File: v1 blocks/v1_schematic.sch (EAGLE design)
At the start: 209 parts, among them IC1 PCA82C250, IC2 FT232RL, IC3 SP3223EBP, IC4 MAX481CPA, IC5 LM2576T, Q1 25MHz, Q2 32.768kHz, Q3 2N2222A, T1 ST02-3.5MM, T3 2N2222, T4 2N2222, T5 2N2222, T6 2N2222, T7 2N2222, U1 ON_SEMICONDUCTOR_NCP1117ST33T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, U2 ON_SEMICONDUCTOR_NCP1117ST50T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, X1 MINI-USB-32005-201, X10 PC817SW, X11 PC817SW, X12 PC817SW, X13 PC817SW, X14 PC817SW, X15 PC817SW, X16 PC817SW, X17 PC817SW, X18 PC817SW, X19 PC817SW, X20 PC817SW, X21 PC817SW, X22 PC817SW, X23 PC817SW, X24 PC817SW, X6 SDBMF, X7 5566-8, X8 5566-8, X9 PC817SW

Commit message: V2
Created new layout template
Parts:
- removed J1: (no value), con-lsta:JBK20
- removed T3, T4, T5, T6, T7: 2N2222, transistor-neu-to92:2N2222
- added H1, H2, H3: MOUNT-PAD-ROUND3.2, holes:MOUNT-PAD-ROUND3.2
- added Q4, Q5, Q6, Q7, Q8: (no value), semicon-smd-ipc:NPN-TRANSISTOR_SOT23
- added U$3: MICROSD-PUSH-OUT, microsd:MICROSD-PUSH-OUT
- X6: value SDBMF -> 5566-20; device farnell:SDBMF -> con-molex:5566-20
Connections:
- net +3V3: now also U$3.VDD, X6-1.S, X6-2.S; no longer J1.1, J1.2, R30.1, R31.1, R32.1, R33.1, R34.2, R35.2, X6.4
- net GND: now also Q8.E, R30.1, R31.1, R32.1, R33.1, R34.2, R35.2, U$3.VSS, X6-10.S, X6-12.S, X6-14.S, X6-16.S, X6-18.S, X6-20.S, X6-4.S, X6-6.S, X6-8.S; no longer J1.10, J1.12, J1.14, J1.16, J1.18, J1.20, J1.4, J1.6, J1.8, T7.E, X6.3, X6.6
- net GND2: now also Q8.C; no longer T7.C
- net N$49: now also Q4.B; no longer T3.B
- net N$50: now also X6-11.S; no longer J1.11
- net N$51: now also Q5.B; no longer T4.B
- net N$52: now also Q6.B; no longer T5.B
- net N$53: now also X6-17.S; no longer J1.17
- net N$54: now also Q7.B; no longer T6.B
- net N$55: now also Q8.B; no longer T7.B
- net N$56: now also X6-19.S; no longer J1.19
- net NRF_SCK: now also X6-13.S; no longer J1.13
- net R1IN: now also Q7.E; no longer T6.E
- net R1IN_: now also Q7.C; no longer T6.C
- net R2IN: now also Q5.E; no longer T4.E
- net R2IN_: now also Q5.C; no longer T4.C
- net RESET#: now also X6-15.S; no longer J1.15
- net SD_CMD: now also U$3.CMD_DIN; no longer X6.2
- net SD_D0: now also U$3.DAT0_DO; no longer X6.7
- net SD_D1: now also U$3.DAT1; no longer X6.8
- net SD_D2: now also U$3.DAT2; no longer X6.9
- net SD_D3: now also U$3.CD_DAT3_CS; no longer X6.1
- net SD_SCK: now also U$3.CLK; no longer X6.5
- net T1OUT: now also Q6.E; no longer T5.E
- net T1OUT_: now also Q6.C; no longer T5.C
- net T2OUT: now also Q4.E; no longer T3.E
- net T2OUT_: now also Q4.C; no longer T3.C
- net TCK/SWCLK: now also X6-9.S; no longer J1.9
- net TDI: now also X6-5.S; no longer J1.5
- net TMS/SWDIO: now also X6-7.S; no longer J1.7
- net TRST: now also X6-3.S; no longer J1.3
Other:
- moved on the sheet: C52, R30, R31, R32, R33, R34, R35

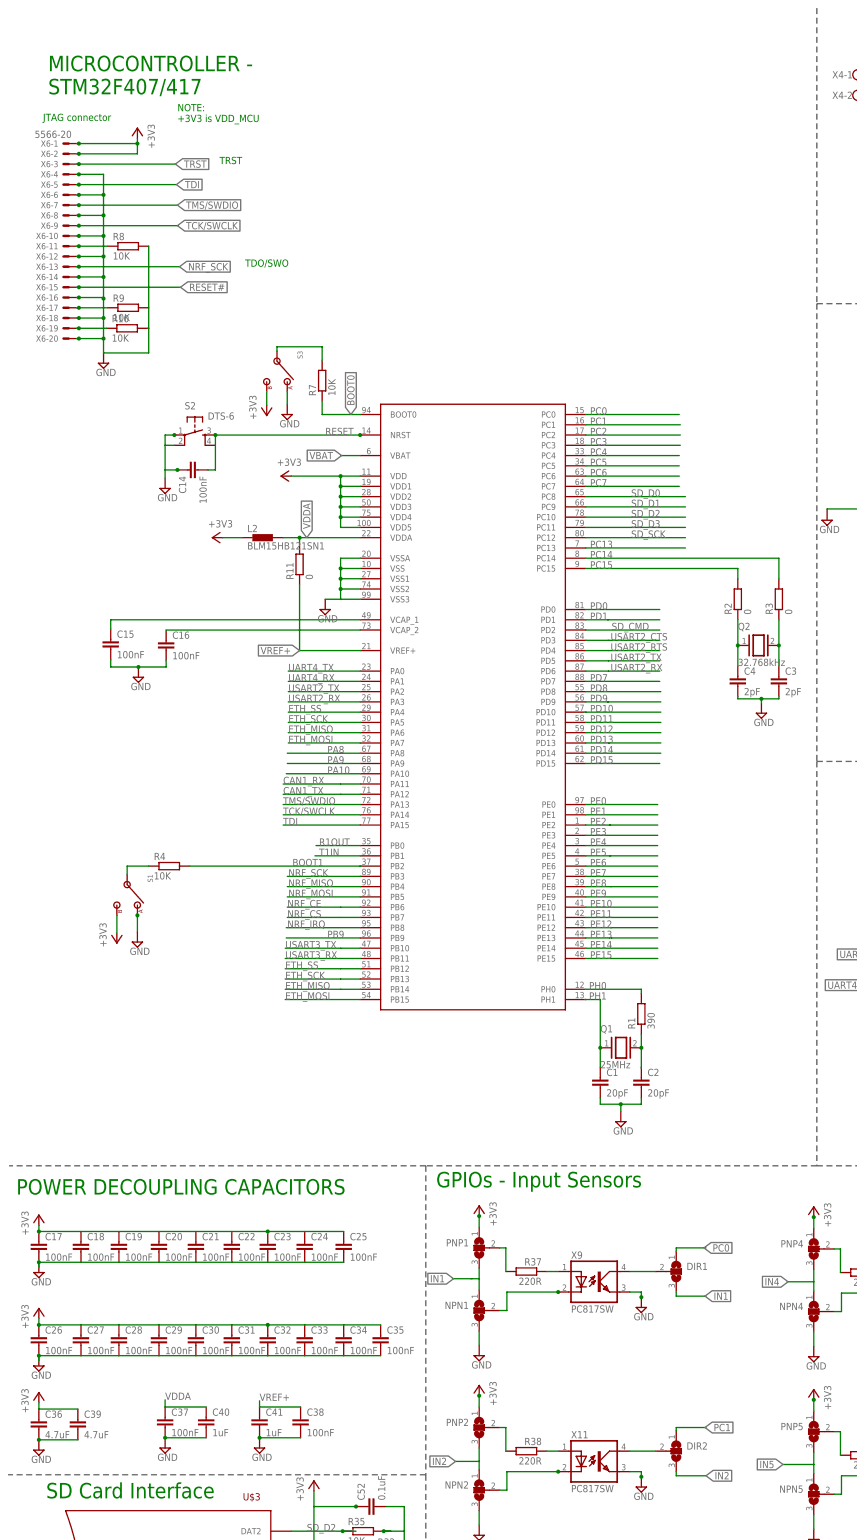
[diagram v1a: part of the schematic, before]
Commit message: UPDATE
Updated design for Main board and I/O
- Reduced form factor, boards will be interconnected using ribbon cable connectors on 20-pin headers
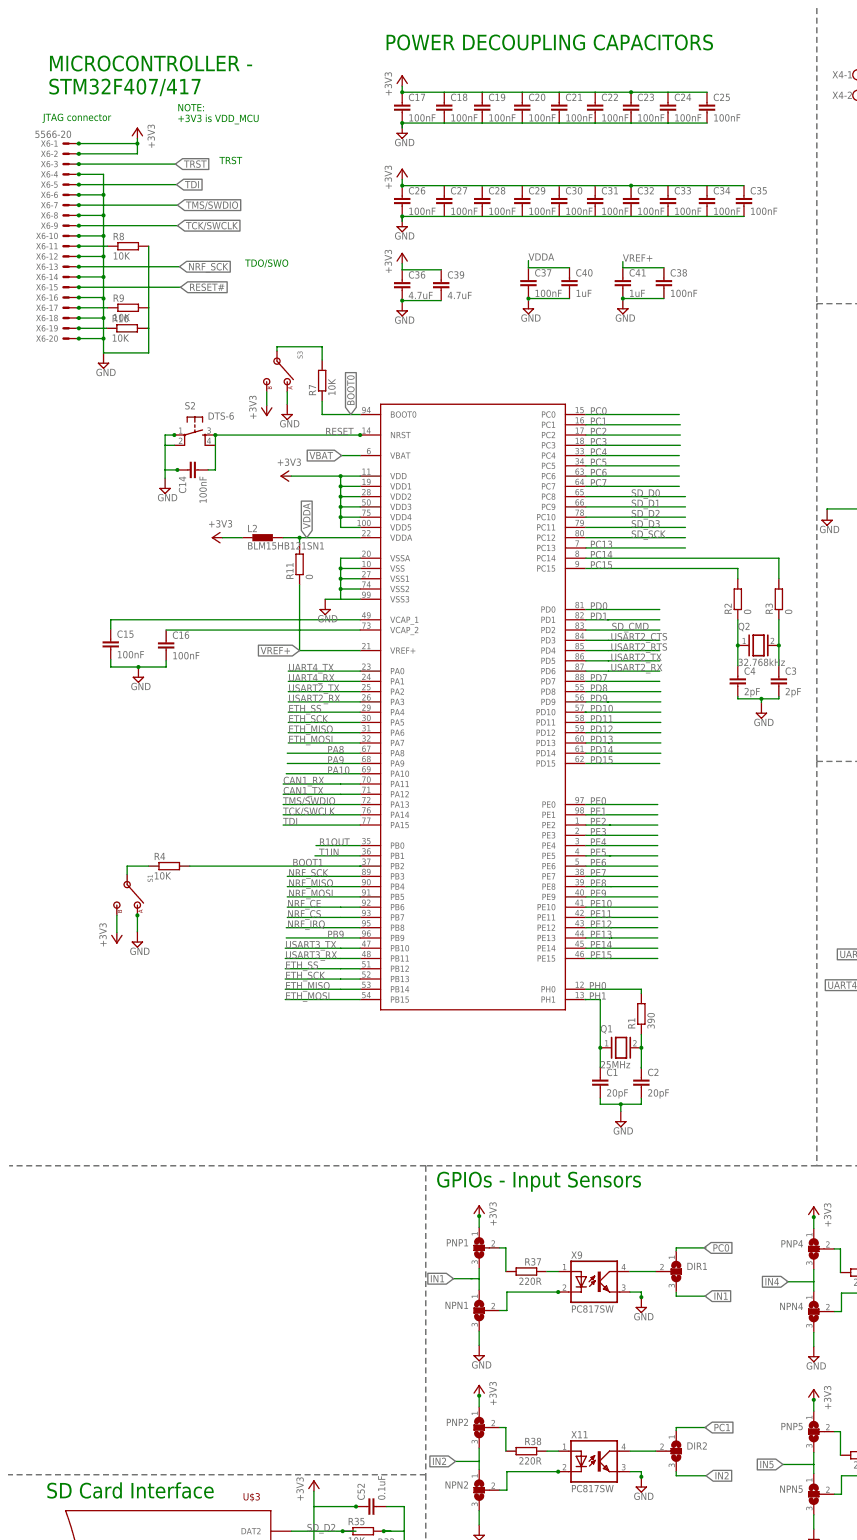
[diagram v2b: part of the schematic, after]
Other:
- moved on the sheet: C17, C18, C19, C20, C21, C22, C23, C24, C25, C26, C27, C28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
